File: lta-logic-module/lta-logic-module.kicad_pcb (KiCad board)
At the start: 2 copper layers, 125 x 89.5 mm, 83 parts, among them J1 Molex-MicroFit_43650-0218, J3 Molex-MicroLatch-53253-1270, J4 Molex-MicroLatch-53253-1270, J5 Molex-MicroLatch-53253-1270, Q1 PT334-6B, Q2 2N3904, SW1 SW_SPST, U1 Feather_M4_Express, U10 SN74LVC00AD, U11 SN74LVC14AD, U12 SN74LVC14AD, U2 LM2595T-5, U3 PCF8574, U4 PCF8574, U5 PCF8574, U6 SN74LVC00AD, U7 SN74LVC00AD, U8 SN74LVC244ADW, U9 SN74LVC00AD

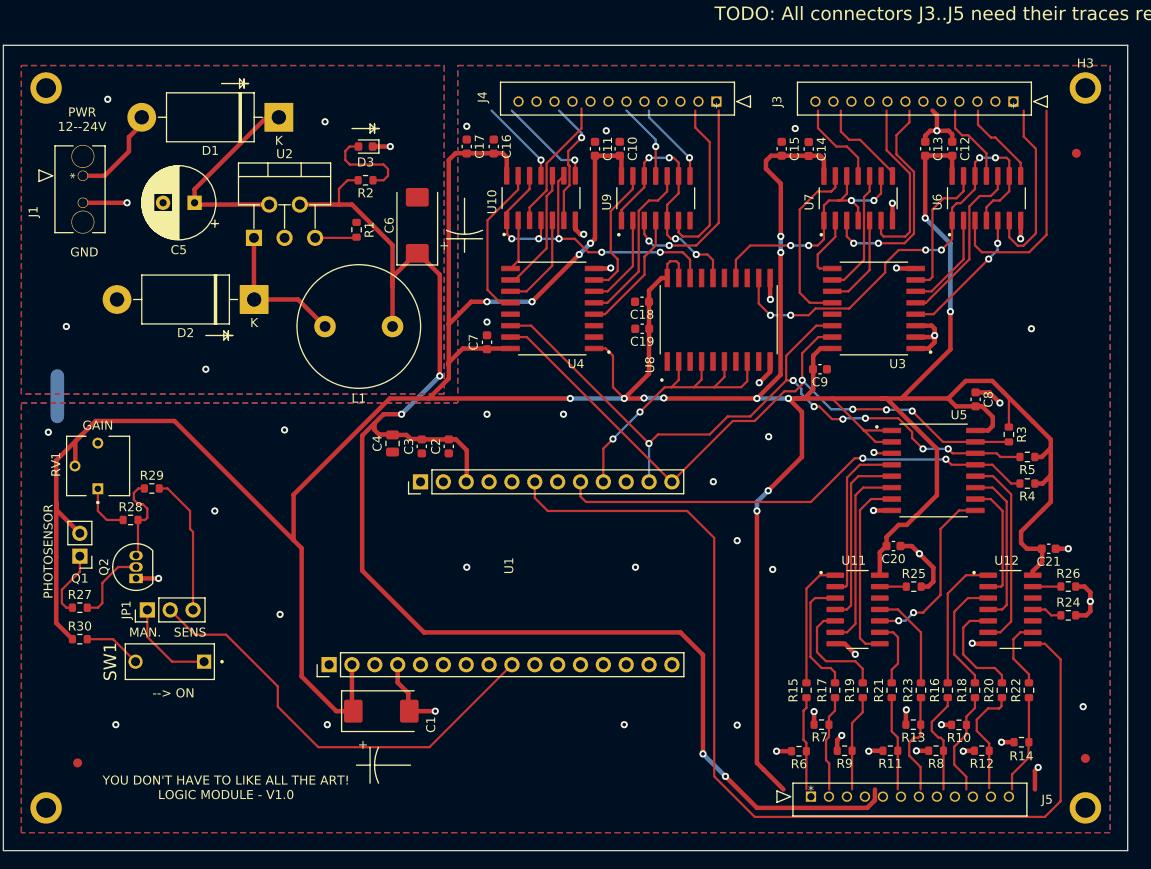
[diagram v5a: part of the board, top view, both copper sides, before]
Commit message: Connect new J3--5 footprints to traces.
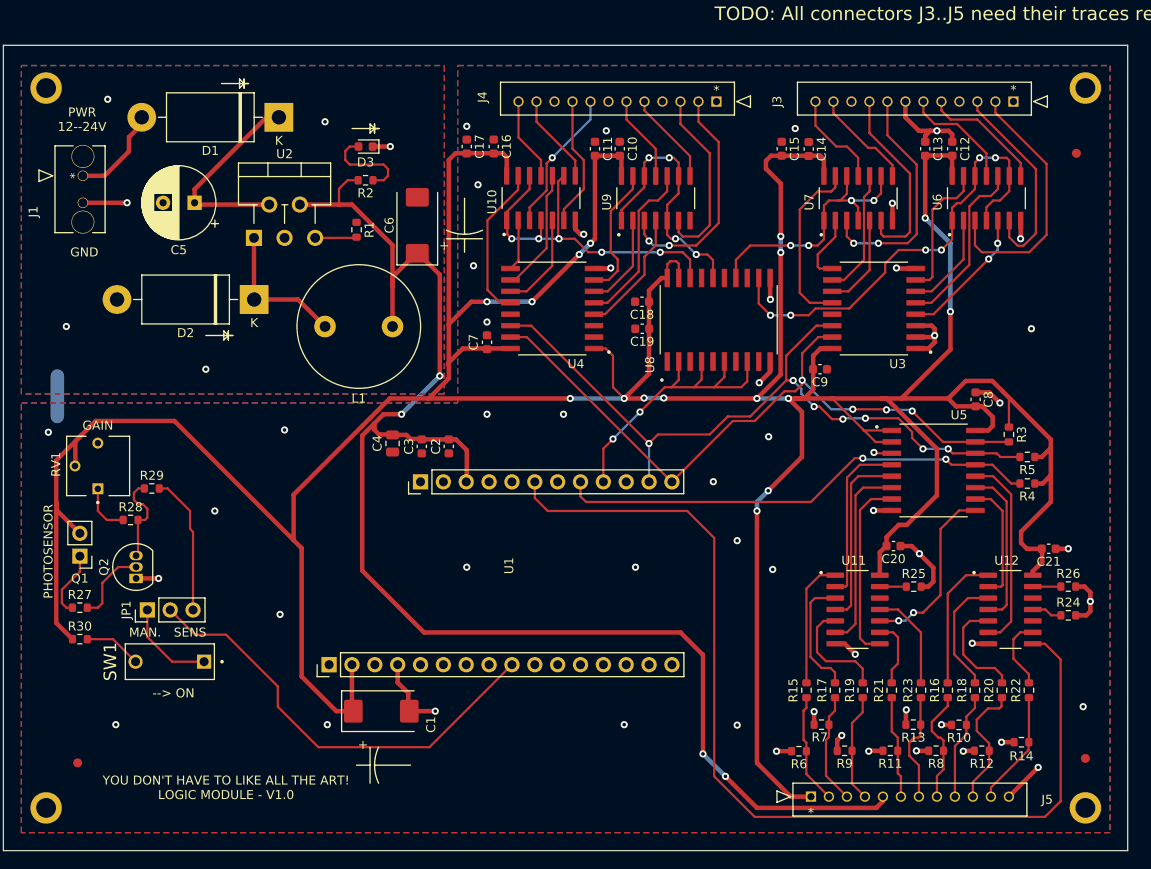
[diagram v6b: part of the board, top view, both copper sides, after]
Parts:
- U2: footprint Package_TO_SOT_THT:TO-220-5_P3.4x3.7mm_StaggerOdd_Lead3.8mm_Vertical -> Aaron_THT:TO-220-5_P3.4x3.7mm_StaggerOdd_Lead3.8mm_Vertical-SilkFix
- U3, U4, U5: value PCF8574 -> PCF8574DW
- U8: value SN74LVC244ADW -> SN74LVC244ADWR
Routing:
- net GND: track 96.5 -> 101.2 mm, vias 57 -> 59
- net /LED Signal Outputs/s2: track 9.53 -> 13.7 mm
- net /LED Signal Outputs/s3: track 9.12 -> 12.6 mm
- net +3V3: track 496.2 -> 499.6 mm
- net /LED Signal Outputs/s0: track 25.6 -> 29.0 mm
- net /LED Signal Outputs/s1: track 20.0 -> 23.1 mm
- net /LED Signal Outputs/s8: track 23.9 -> 25.9 mm
- net /Button Inputs/btn_in0: track 10.5 -> 12.3 mm
- net /LED Signal Outputs/s5: track 19.6 -> 21.4 mm
- net /Button Inputs/btn_in8: track 11.2 -> 12.9 mm
- net /Button Inputs/btn_in7: track 12.5 -> 14.1 mm
- net /LED Signal Outputs/s9: track 18.9 -> 20.6 mm
- net /Button Inputs/btn_in1: track 10.8 -> 12.4 mm
- net /LED Signal Outputs/s6: track 9.94 -> 11.5 mm
- net /Button Inputs/btn_in2: track 10.7 -> 12.1 mm
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
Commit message: All DRC checks passing.
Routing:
- net GND: track 101.2 -> 119.8 mm, vias 59 -> 75
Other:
- board text removed: "TODO: All connectors J3..J5 need their traces realigned"

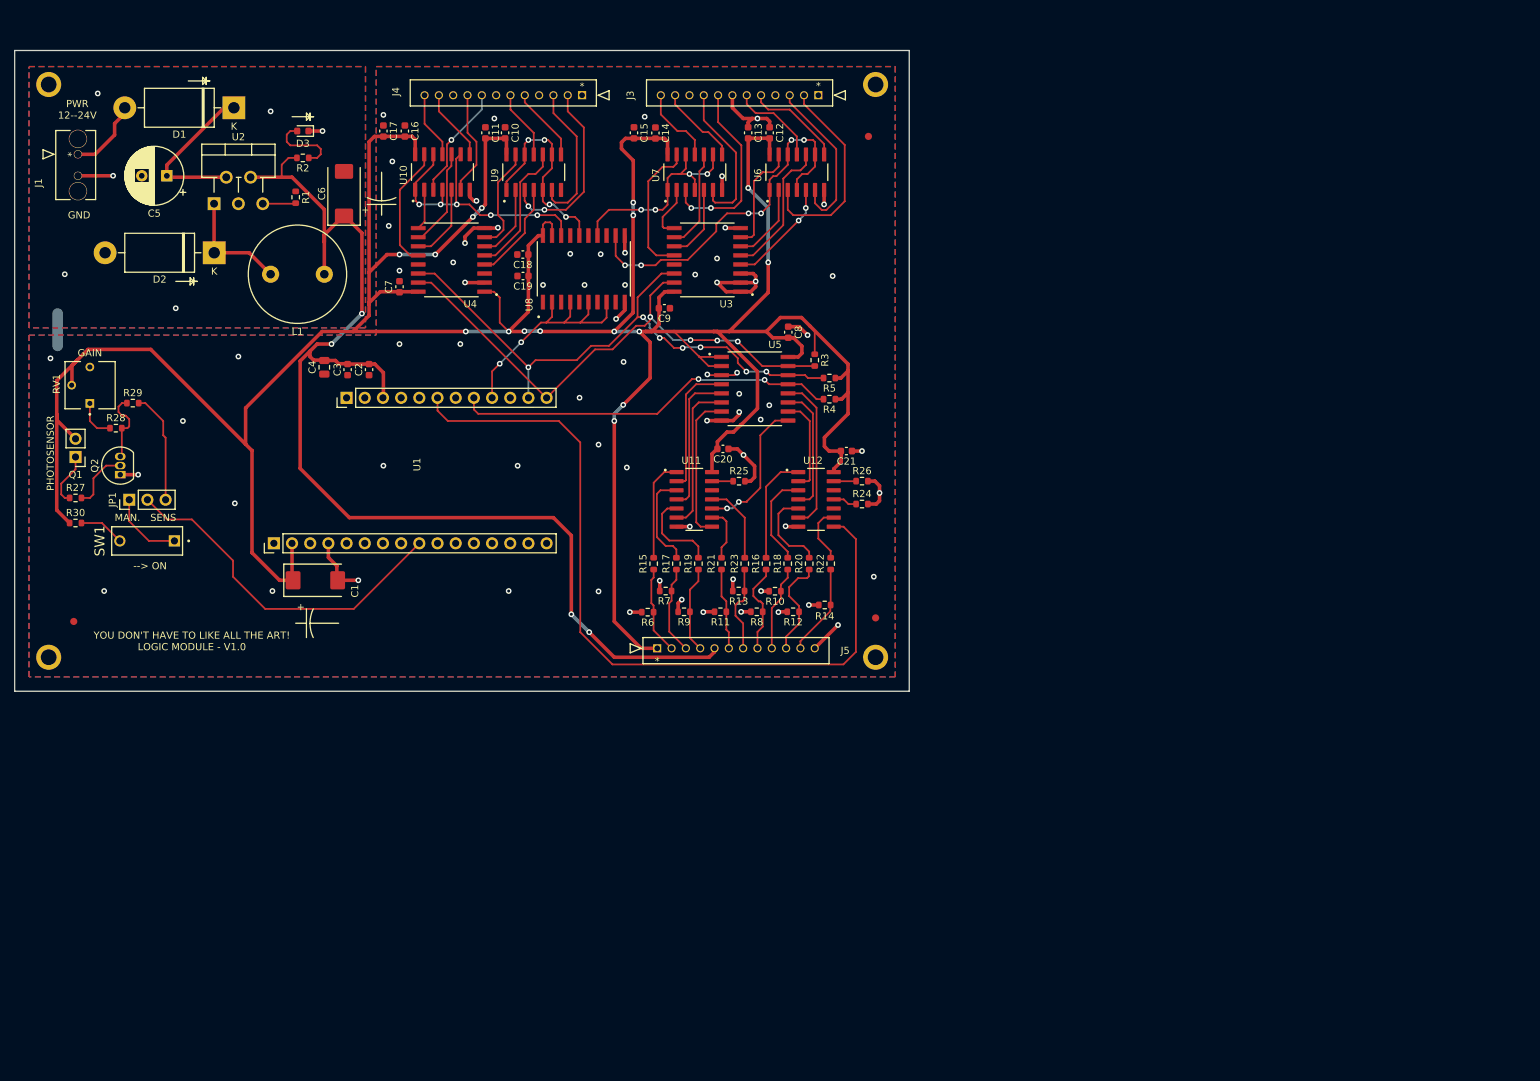
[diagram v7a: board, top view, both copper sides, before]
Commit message: Update some footprints to be more accurate.
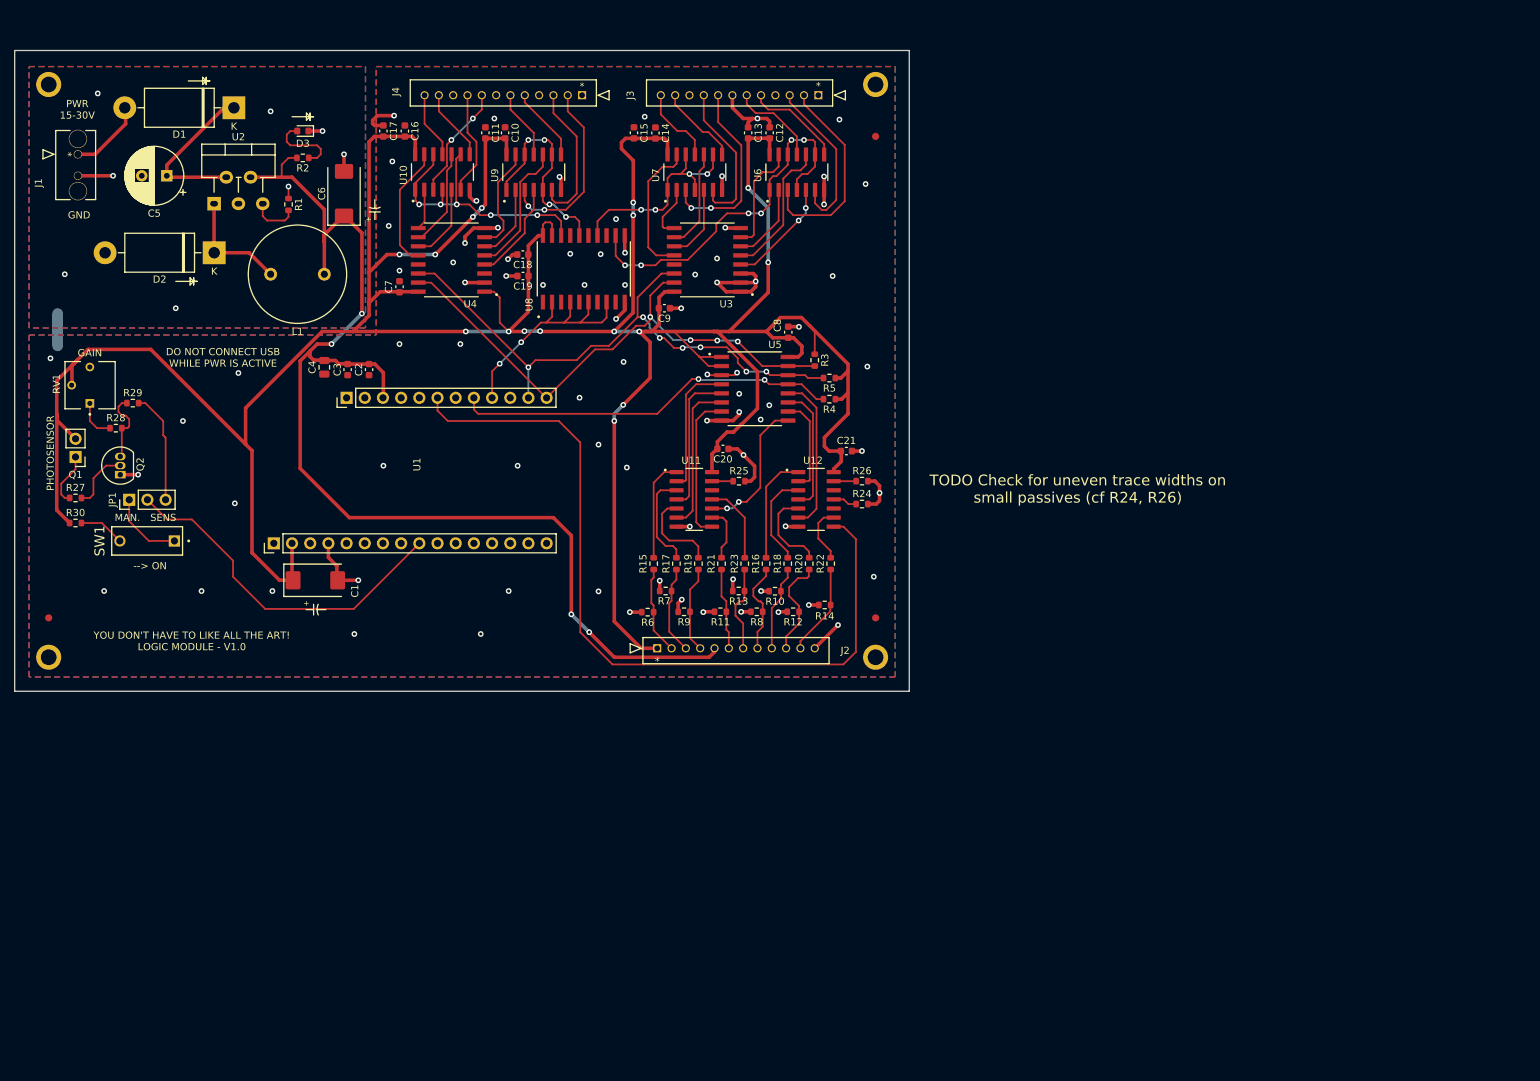
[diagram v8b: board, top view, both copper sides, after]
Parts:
- moved FID1 3.54 mm to (21.8, 96.8)
- moved R1 1.41 mm to (55.3, 39.0)
- moved FID3 1.00 mm to (137.3, 29.5)
- renumbered J5 to J2
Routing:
- net GND: track 119.8 -> 136.0 mm, vias 75 -> 89
- net Net-(R1-Pad2): track 4.70 -> 6.81 mm
- net Net-(D1-Pad2): track 10.0 -> 10.9 mm
- net /LED Signal Outputs/s12: vias 1 -> 2
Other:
- board text added: "DO NOT CONNECT USB WHILE PWR IS ACTIVE"
- board text added: "PWR 15-30V"
- board text added: "TODO Check for uneven trace widths on small passives (cf R24, R26)"
- board text removed: "PWR 12--24V"
